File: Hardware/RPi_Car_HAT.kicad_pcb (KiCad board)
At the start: 2 copper layers, 65 x 56 mm, 43 parts, among them J1 Conn_01x04, J2 Conn_01x02, J3 40HAT, J4 USB_A, Q1 2N3904, Q2 2N3904, Q3 2N3904, Q4 IRF9540N, U1 PC817, U2 PC817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

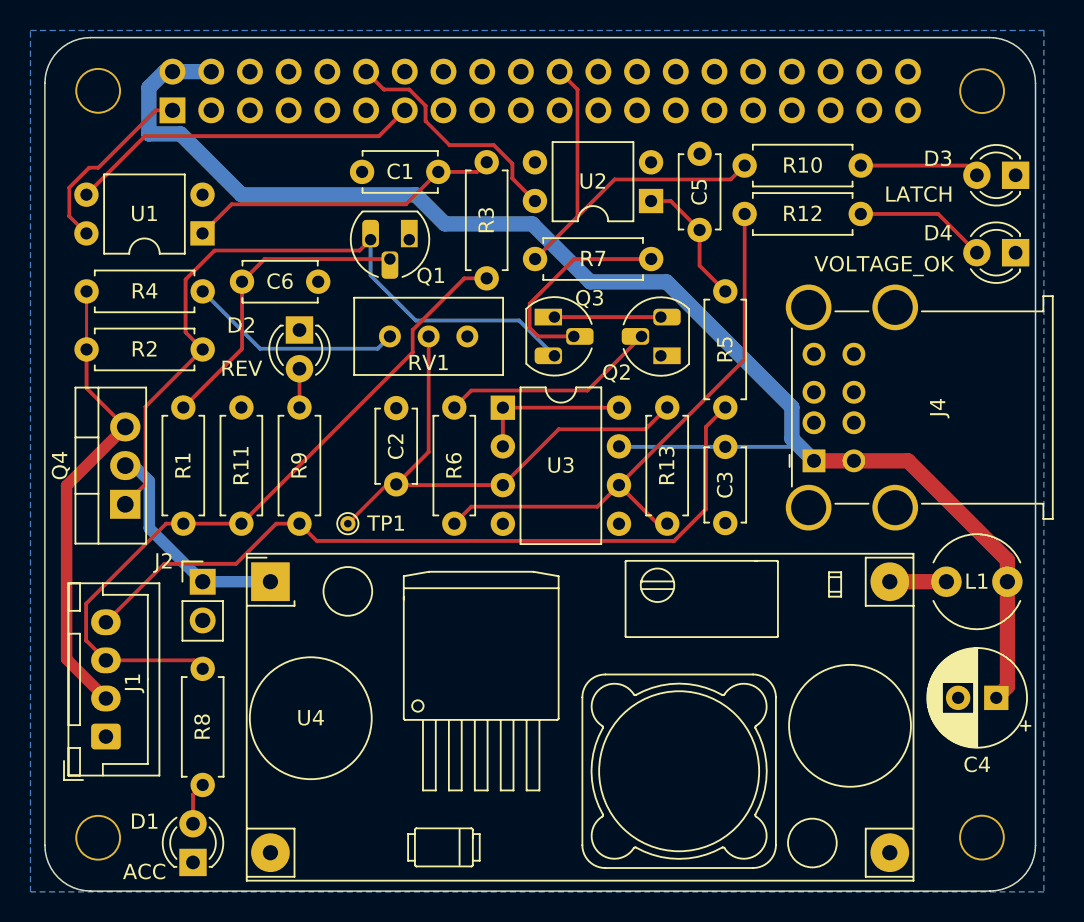
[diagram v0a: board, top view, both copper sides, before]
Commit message: Low voltage cut-off: add hysteresis, increase RC-time
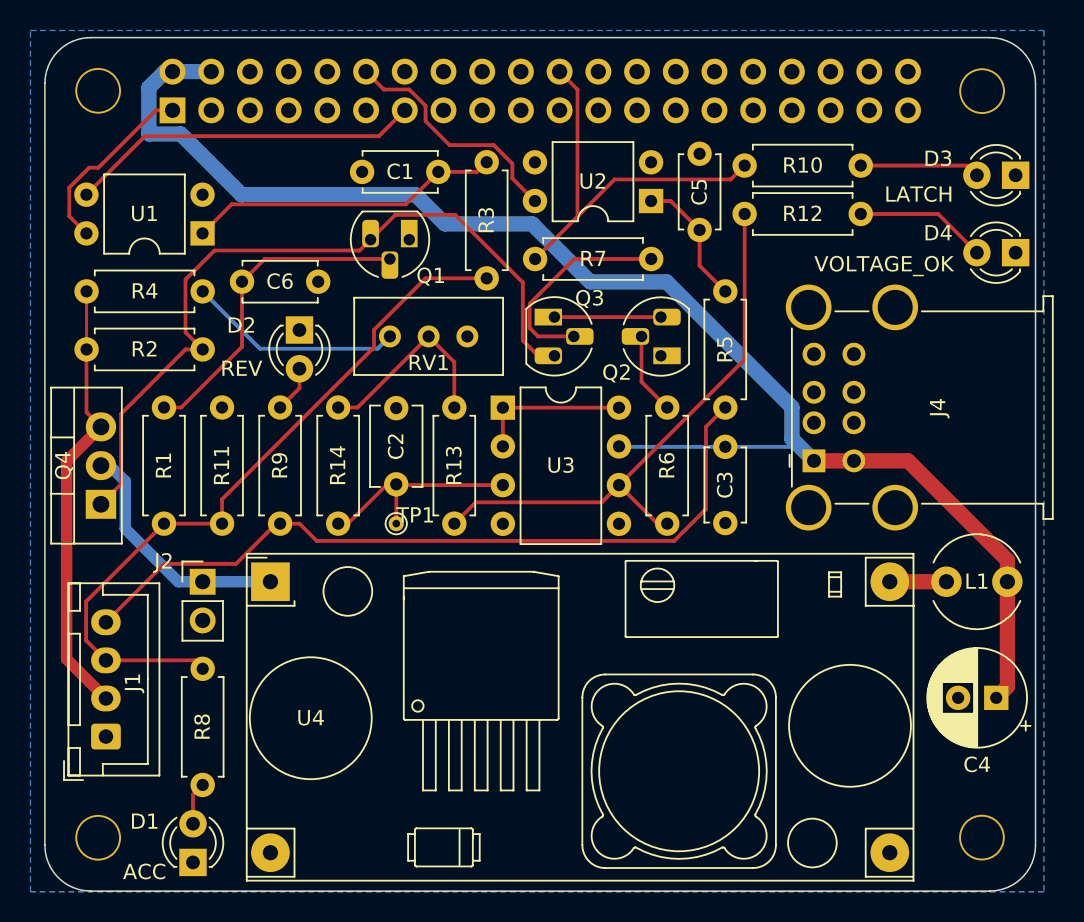
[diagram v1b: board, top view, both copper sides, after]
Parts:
- added R14: 250k, Resistor_THT:R_Axial_DIN0207_L6.3mm_D2.5mm_P7.62mm_Horizontal, F.Cu at (97.8, 85.1)
- C2: value 0.1 uF -> 10 uF; footprint Capacitor_THT:C_Disc_D4.7mm_W2.5mm_P5.00mm -> Capacitor_THT:C_Disc_D5.1mm_W3.2mm_P5.00mm
- moved R13 14.0 mm to (105.4, 92.7)
- moved R6 14.0 mm to (119.4, 92.7)
- moved TP1 3.17 mm to (101.6, 92.7)
- moved Q4 1.59 mm to (82.2, 91.4)
- moved R1 1.27 mm to (86.4, 92.7)
- moved R11 1.27 mm to (90.2, 92.7)
- moved R9 1.27 mm to (94.0, 92.7)
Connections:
- R13 pad 2: Net-(C2-Pad1) -> Net-(R13-Pad2)
- RV1 pad 2: Net-(C2-Pad1) -> Net-(R13-Pad2)
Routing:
- net Net-(C2-Pad1): track 34.7 -> 13.8 mm
- net Net-(R13-Pad2): track 0.00 -> 13.2 mm
- net Net-(Q2-Pad2): track 14.2 -> 5.36 mm
- net Net-(Q1-Pad3): track 47.1 -> 50.7 mm
- net Net-(C6-Pad1): track 19.5 -> 21.4 mm
- net /BAT_SW: track 14.5 -> 16.1 mm
- net /BAT: track 30.4 -> 29.1 mm
- net /ACC: track 46.8 -> 47.7 mm
- net Net-(D2-Pad2): track 2.55 -> 3.07 mm

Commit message: Put ACC trigger behind low voltage cut-off, update to new KiCAD version
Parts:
- moved Q3 2.71 mm to (112.9, 81.7), turned to 90 degrees
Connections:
- Q1 pad 1: GND -> Net-(Q1-E)
- Q2 pad 3: Net-(Q2-Pad3) -> Net-(Q1-E)
- Q3 pad 1: Net-(Q2-Pad3) -> Net-(Q1-E)
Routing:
- net Net-(Q1-E): track 0.00 -> 23.0 mm
- net Net-(Q2-Pad3): track 6.98 -> 0.00 mm
- net Net-(Q3-B): track 13.9 -> 9.11 mm
- net Net-(Q1-C): track 50.7 -> 48.3 mm

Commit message: Revert "Put ACC trigger behind low voltage cut-off, update to new KiCAD version"
This reverts commit 32efec27a2ba4a602edbb2af9725aed434bd226d.
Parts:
- moved Q3 2.71 mm to (112.0, 79.2), turned to -90 degrees
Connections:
- Q1 pad 1: Net-(Q1-E) -> GND
- Q2 pad 3: Net-(Q1-E) -> Net-(Q2-Pad3)
- Q3 pad 1: Net-(Q1-E) -> Net-(Q2-Pad3)
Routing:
- net Net-(Q1-E): track 23.0 -> 0.00 mm
- net Net-(Q2-Pad3): track 0.00 -> 6.98 mm
- net Net-(Q3-Pad2): track 9.11 -> 13.9 mm
- net Net-(Q1-Pad3): track 48.3 -> 50.7 mm
